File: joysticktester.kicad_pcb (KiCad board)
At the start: 2 copper layers, 100 x 65 mm, 18 parts, among them J1 USB_OTG, J2 DB9_Male

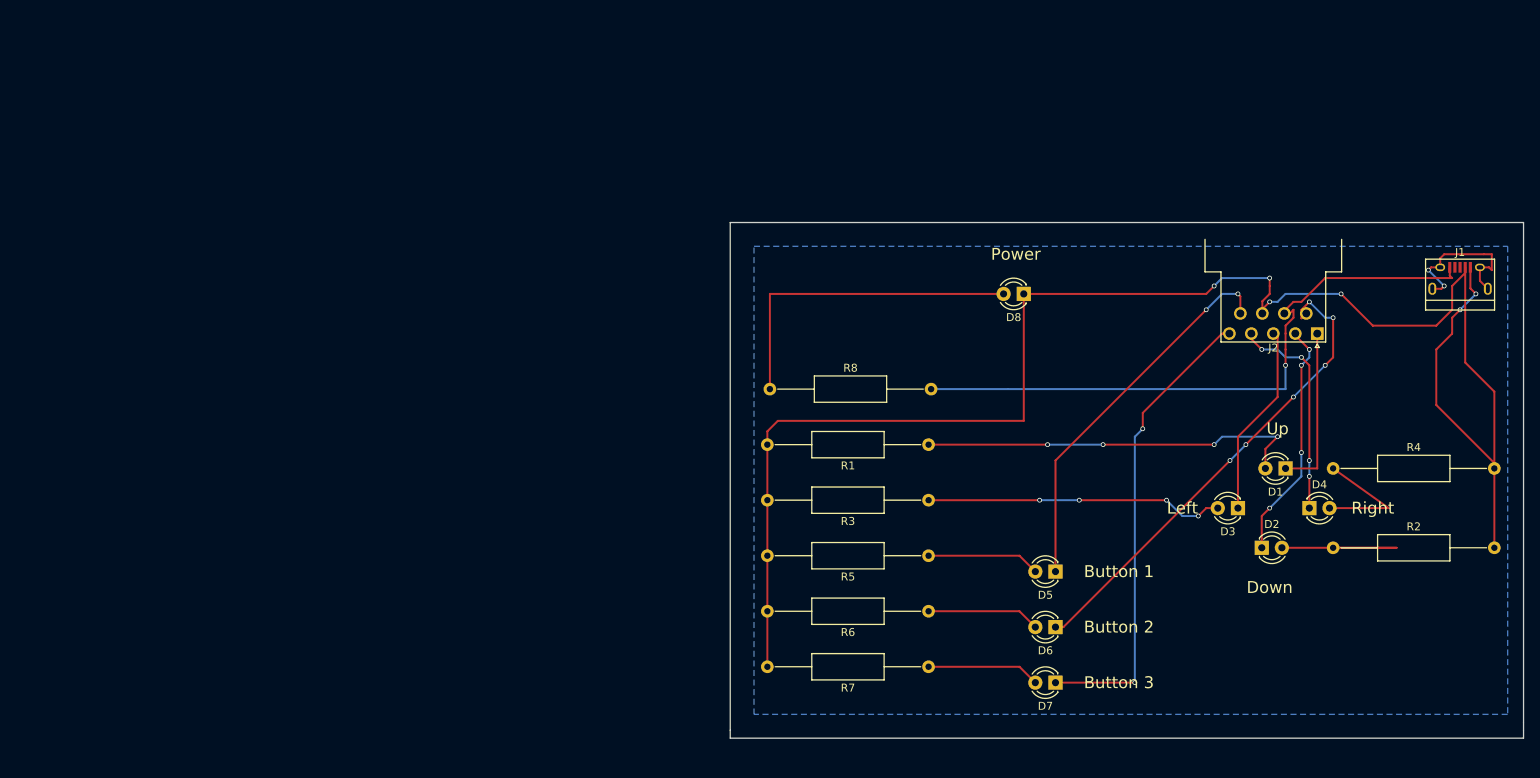
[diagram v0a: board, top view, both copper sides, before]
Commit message: fix led connection
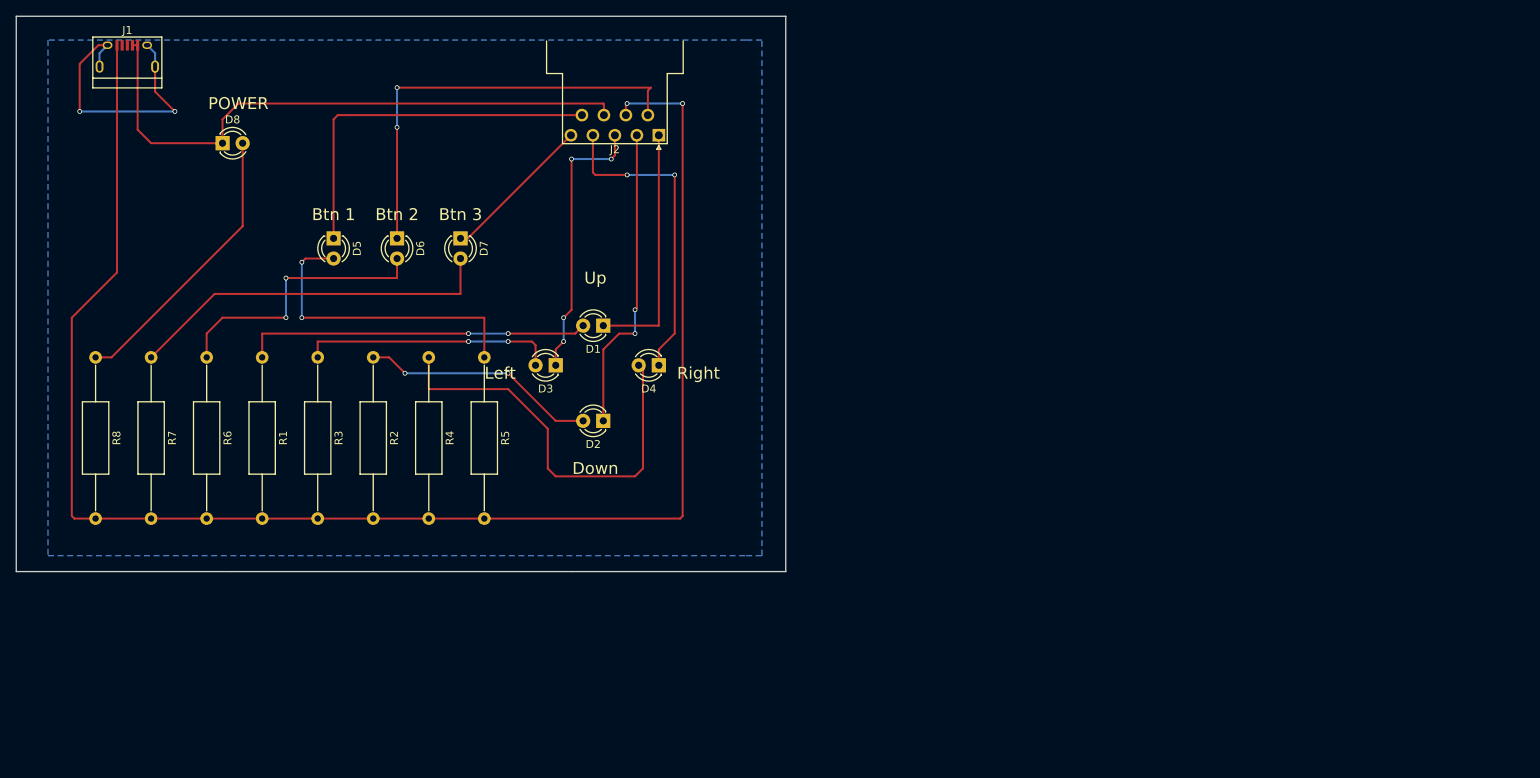
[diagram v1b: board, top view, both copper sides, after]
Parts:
- moved J1 170.3 mm to (52.0, 31.0)
- moved R2 123.4 mm to (83.0, 69.0), turned to 270 degrees
- moved R4 114.9 mm to (90.0, 69.0), turned to 270 degrees
- moved R7 105.5 mm to (55.0, 69.0), turned to 270 degrees
- moved D8 102.8 mm to (64.0, 42.0), turned to 0 degrees
- moved D5 100.2 mm to (78.0, 54.0), turned to 270 degrees
- moved R6 96.5 mm to (62.0, 69.0), turned to 270 degrees
- moved D6 96.4 mm to (86.0, 54.0), turned to 270 degrees
- moved D7 93.6 mm to (94.0, 54.0), turned to 270 degrees
- moved D1 87.9 mm to (112.0, 65.0)
- moved D3 87.9 mm to (106.0, 70.0)
- moved J2 86.7 mm to (119.0, 41.0)
- moved R8 85.1 mm to (48.0, 69.0), turned to 270 degrees
- moved R1 84.7 mm to (69.0, 69.0), turned to 270 degrees
- moved D2 84.5 mm to (112.0, 77.0), turned to 180 degrees
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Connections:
- R1 pad 2: /GROUND -> /VCC
- R2 pad 2: /GROUND -> /VCC
- R3 pad 2: /GROUND -> /VCC
- R4 pad 2: /GROUND -> /VCC
- R5 pad 2: /GROUND -> /VCC
- R6 pad 2: /GROUND -> /VCC
- R7 pad 2: /GROUND -> /VCC
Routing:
- net /GROUND: track 216.6 -> 76.0 mm, vias 6 -> 0
- net /VCC: track 81.7 -> 199.5 mm, vias 1 -> 2
- net /BUTTON3: track 59.5 -> 19.3 mm, vias 2 -> 0
- net Net-(D4-Pad2): track 16.1 -> 52.1 mm
- net Net-(D7-Pad2): track 14.3 -> 46.8 mm
- net Net-(D5-Pad2): track 14.3 -> 39.2 mm, vias 0 -> 2
- net Net-(D6-Pad2): track 14.3 -> 35.3 mm, vias 0 -> 2
- net Net-(J1-Pad6): track 20.7 -> 35.4 mm
- net /RIGHT: track 27.4 -> 40.0 mm, vias 4 -> 2
- net /LEFT: track 24.3 -> 35.0 mm, vias 0 -> 4
- net /UP: track 21.0 -> 31.0 mm
- net /DOWN: track 30.2 -> 38.9 mm, vias 4 -> 2
- net Net-(D2-Pad2): track 22.5 -> 29.8 mm, vias 0 -> 2
- net /BUTTON2: track 61.3 -> 54.6 mm, vias 7 -> 2
- net Net-(D8-Pad2): track 41.5 -> 35.9 mm
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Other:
- board size 100 x 65 mm -> 97 x 70 mm
- rule pad_to_mask_clearance: 0.2 -> 0
- board text added: "Btn 1"
- board text added: "Btn 2"
- board text added: "Btn 3"
- board text added: "POWER"
- board text added: "https://github.com/Ozzyboshi/AmigaJoystickTesterPCB"
- board text removed: "Button 1"
- board text removed: "Button 2"
- board text removed: "Button 3"
- board text removed: "Power"
- board text removed: "https://github.com/Ozzyboshi/AmigaJoystickTesterPCB.git"

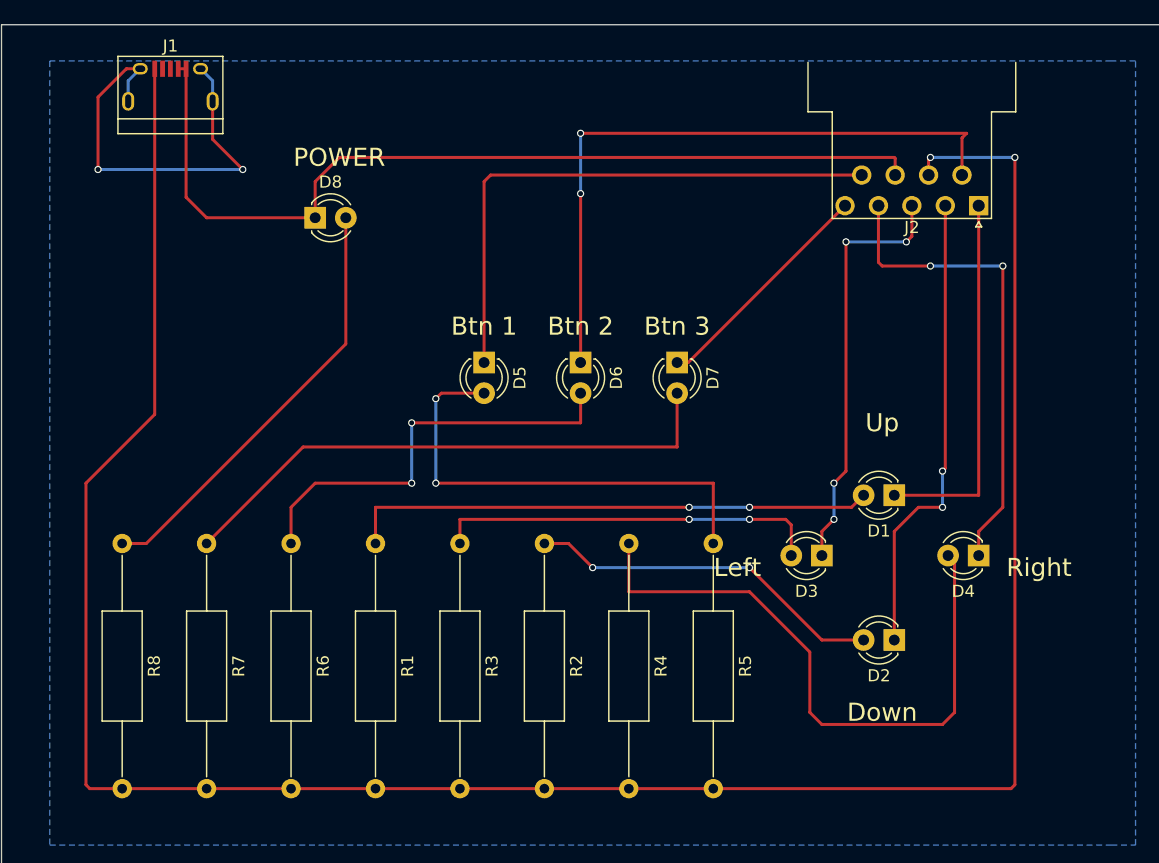
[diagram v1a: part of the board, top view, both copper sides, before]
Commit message: rotated usb connector
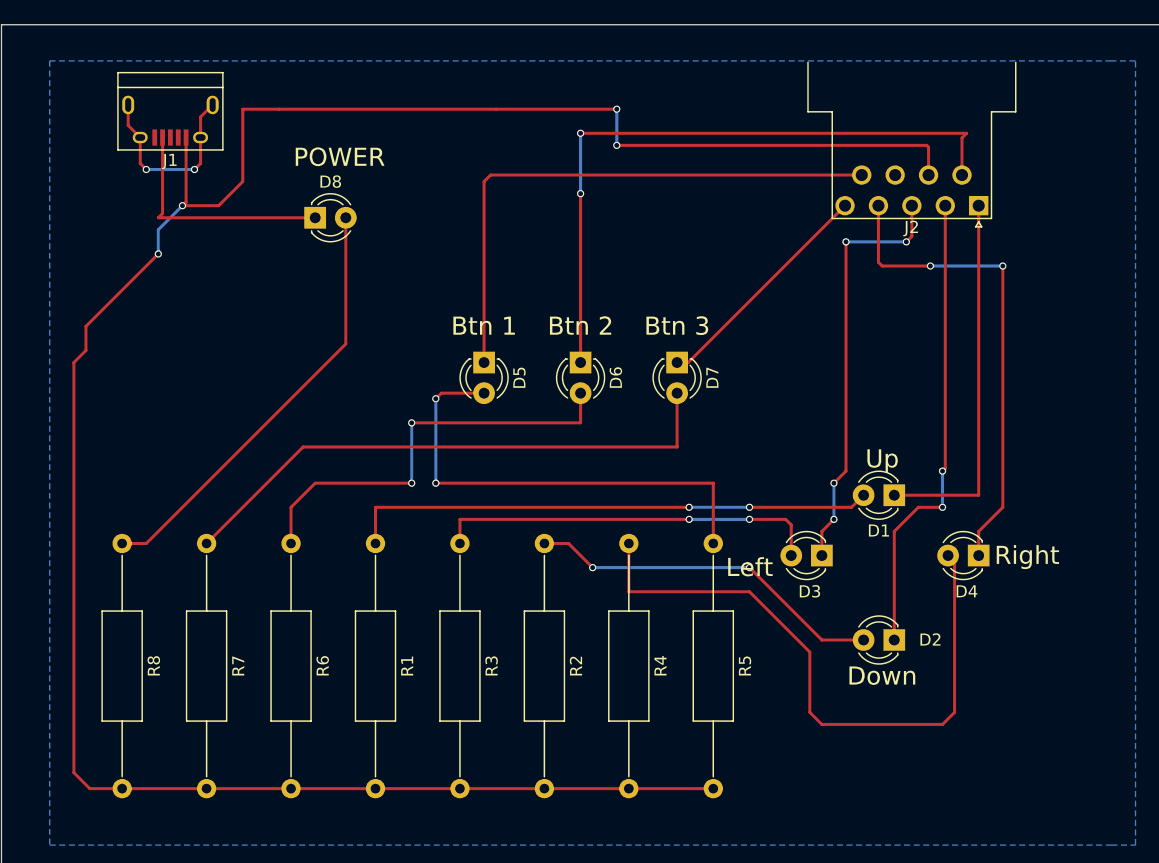
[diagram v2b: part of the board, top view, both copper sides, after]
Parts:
- moved J1 3.00 mm to (52.0, 34.0), turned to 180 degrees
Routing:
- net /GROUND: track 76.0 -> 19.8 mm
- net Net-(J1-Pad6): track 35.4 -> 15.9 mm
- net /VCC: track 199.5 -> 184.1 mm, vias 2 -> 4

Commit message: new db9 connector
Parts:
- removed J2: DB9_Male, Connectors_DSub:DSUB-9_Male_Horizontal_Pitch2.77x2.54mm_EdgePinOffset9.40mm
- added J3: DB-9, w_conn_d-sub:DB_9M, F.Cu at (103.0, 61.0)
- moved R7 90.0 mm to (133.0, 114.0), turned to 0 degrees
- moved R8 86.7 mm to (133.0, 86.0), turned to 0 degrees
- moved R1 84.1 mm to (153.0, 72.0), turned to 180 degrees
- moved R6 71.1 mm to (133.0, 65.0), turned to 0 degrees
- moved J1 68.0 mm to (75.0, 98.0), turned to 270 degrees
- moved D7 61.2 mm to (106.0, 114.0), turned to 0 degrees
- moved D6 60.5 mm to (94.0, 114.0), turned to 0 degrees
- moved D5 60.1 mm to (82.0, 114.0), turned to 0 degrees
- moved R2 58.8 mm to (133.0, 100.0), turned to 0 degrees
- moved R3 57.9 mm to (133.0, 79.0), turned to 0 degrees
- moved R5 52.3 mm to (133.0, 107.0), turned to 0 degrees
- moved R4 49.2 mm to (133.0, 93.0), turned to 0 degrees
- moved D8 38.3 mm to (77.0, 78.0)
- moved D3 27.8 mm to (92.0, 94.0), turned to 0 degrees
- moved D2 26.8 mm to (100.0, 101.0), turned to 0 degrees
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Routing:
- net /BUTTON3: track 19.3 -> 93.7 mm, vias 0 -> 2
- net /GROUND: track 19.8 -> 73.1 mm, vias 0 -> 4
- net /BUTTON1: track 46.5 -> 83.9 mm, vias 0 -> 8
- net /UP: track 31.0 -> 66.2 mm, vias 0 -> 2
- net Net-(D6-Pad2): track 35.3 -> 70.4 mm, vias 2 -> 4
- net /BUTTON2: track 54.6 -> 81.8 mm, vias 2 -> 8
- net Net-(D4-Pad2): track 52.1 -> 28.3 mm
- net Net-(D7-Pad2): track 46.8 -> 24.5 mm
- net Net-(D8-Pad2): track 35.9 -> 57.6 mm, vias 0 -> 2
- net Net-(D1-Pad2): track 43.9 -> 61.4 mm
- net /DOWN: track 38.9 -> 54.4 mm
- net /LEFT: track 35.0 -> 47.7 mm, vias 4 -> 2
- net Net-(D5-Pad2): track 39.2 -> 51.7 mm, vias 2 -> 0
- net Net-(D3-Pad2): track 32.2 -> 44.7 mm
- net /RIGHT: track 40.0 -> 44.9 mm, vias 2 -> 0
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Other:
- board size 97 x 70 mm -> 100 x 70 mm
- board text added: "DOWN"
- board text added: "LEFT"
- board text added: "RIGHT"
- board text added: "UP"
- board text removed: "Btn 1"
- board text removed: "Btn 2"
- board text removed: "Btn 3"
- board text removed: "Down"
- board text removed: "Left"
- board text removed: "POWER"
- board text removed: "Right"
- board text removed: "Up"
- board text removed: "https://github.com/Ozzyboshi/AmigaJoystickTesterPCB"

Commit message: new silk back
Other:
- board text added: "https://github.com/Ozzyboshi/AmigaJoystickTesterPCB"
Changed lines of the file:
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@@
     (links 30)
     (no_connects 0)
-    (area 71.949999 49.949999 172.050001 121.050001)
+    (area 70.949999 49.949999 171.050001 120.050001)
     (thickness 1.6)
-    (drawings 8)
+    (drawings 9)
     (tracks 201)
     (zones 0)
@@
     )
   )
+  (gr_text https://github.com/Ozzyboshi/AmigaJoystickTesterPCB (at 124 85) (layer B.SilkS)
+    (effects (font (size 1.5 1.5) (thickness 0.3)) (justify mirror))
+  )
   (gr_line (start 171 50) (end 71 50) (angle 90) (layer Edge.Cuts) (width 0.1))

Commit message: added btn desc
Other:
- board text added: "Button 1"
- board text added: "Button 2"
- board text added: "Button 3"
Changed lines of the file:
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@@
     (area 70.949999 49.949999 171.050001 120.050001)
     (thickness 1.6)
-    (drawings 9)
+    (drawings 12)
     (tracks 201)
     (zones 0)
@@
     )
   )
+  (gr_text "Button 3" (at 107 118) (layer F.Cu)
+    (effects (font (size 1.5 1.5) (thickness 0.3)))
+  )
+  (gr_text "Button 2" (at 95 118) (layer F.Cu)
+    (effects (font (size 1.5 1.5) (thickness 0.3)))
+  )
+  (gr_text "Button 1" (at 83 118) (layer F.Cu)
+    (effects (font (size 1.5 1.5) (thickness 0.3)))
+  )
   (gr_text https://github.com/Ozzyboshi/AmigaJoystickTesterPCB (at 124 85) (layer B.SilkS)

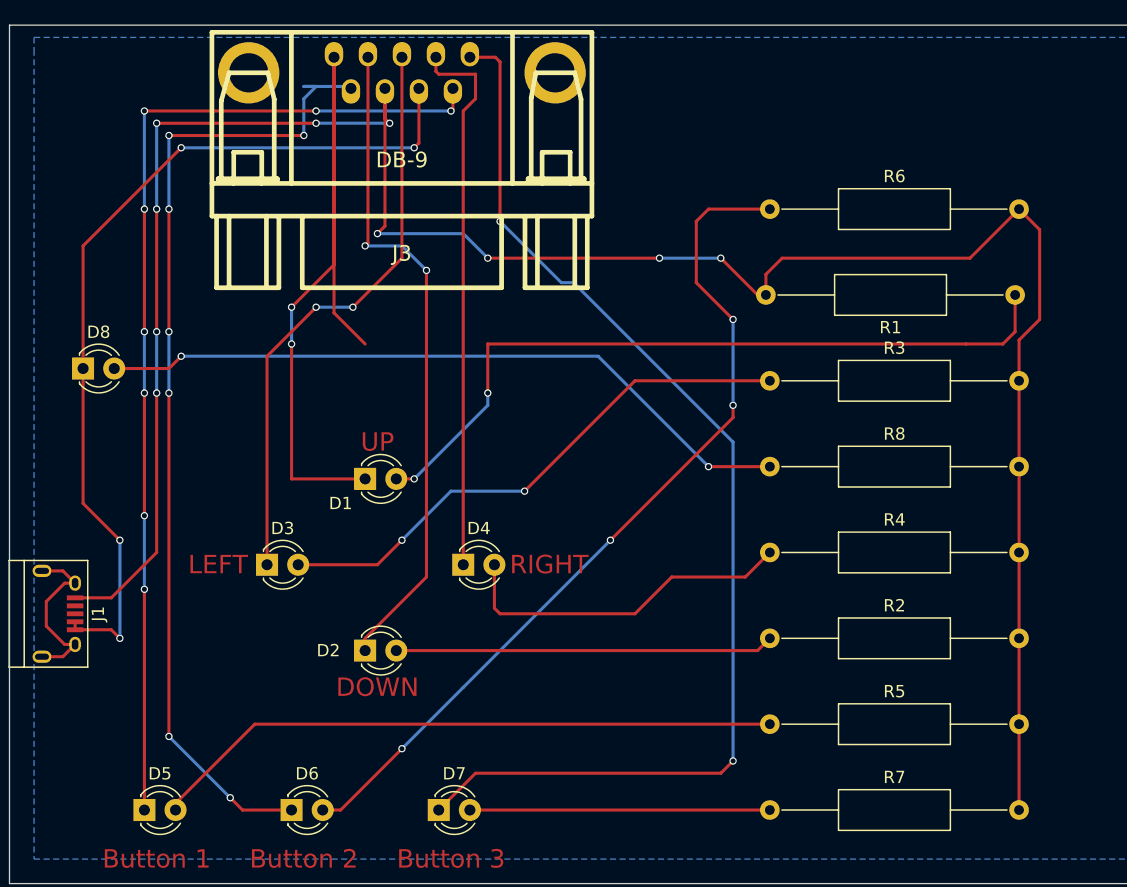
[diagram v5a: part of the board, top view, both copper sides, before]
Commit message: change db9 direction
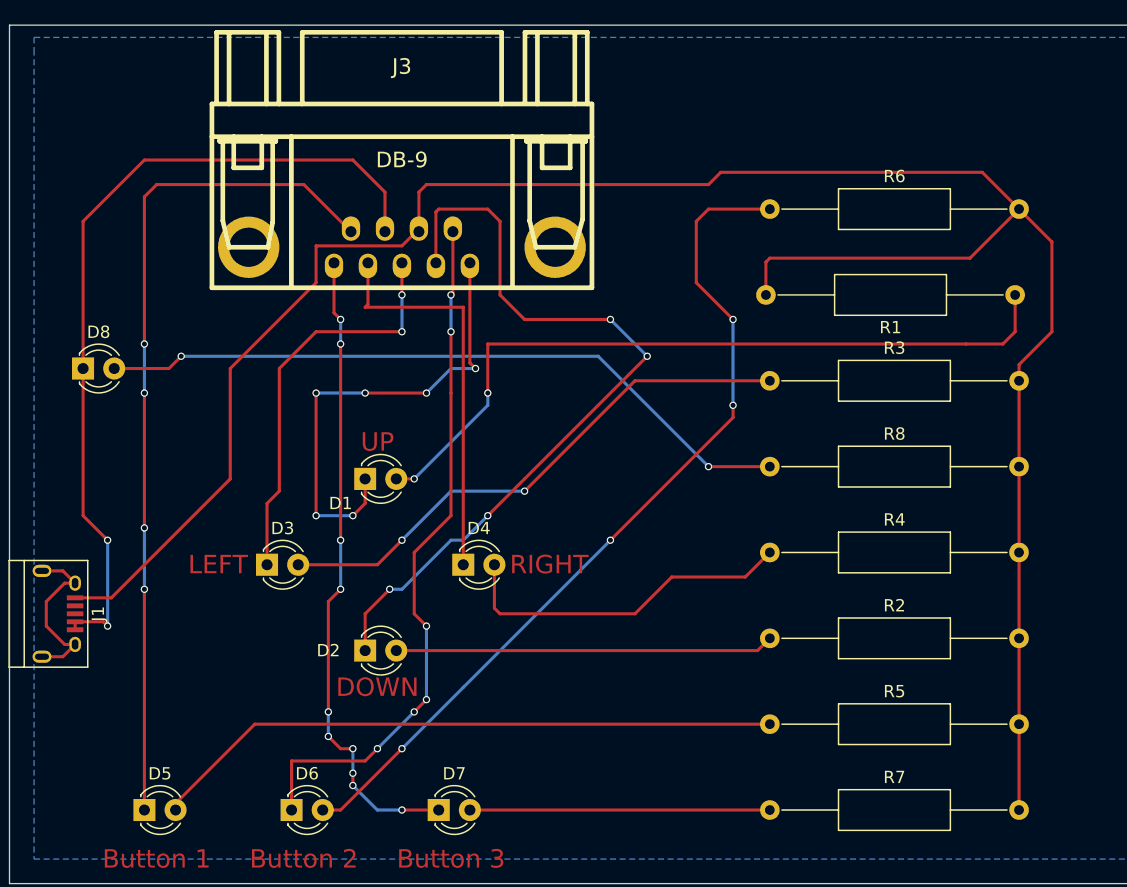
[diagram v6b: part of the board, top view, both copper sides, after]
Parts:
- turned J3 to 180 degrees
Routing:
- net /BUTTON3: track 93.7 -> 52.5 mm, vias 2 -> 10
- net /UP: track 66.2 -> 39.1 mm, vias 2 -> 6
- net /BUTTON2: track 81.8 -> 57.0 mm, vias 8 -> 6
- net /BUTTON1: track 83.9 -> 68.9 mm, vias 8 -> 4
- net /LEFT: track 47.7 -> 33.3 mm
- net /RIGHT: track 44.9 -> 32.7 mm
- net /DOWN: track 54.4 -> 64.7 mm, vias 2 -> 4
- net /VCC: track 185.9 -> 177.8 mm, vias 10 -> 0
- net /GROUND: track 73.1 -> 68.3 mm, vias 4 -> 2
